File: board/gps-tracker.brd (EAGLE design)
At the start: 52.1 x 77.5 mm, 30 parts, among them J2 AVR_SPI_PRG_6OFFSET_PADS, U2 MCP73831, U3 ATMEGA328P, X1 USBSMD

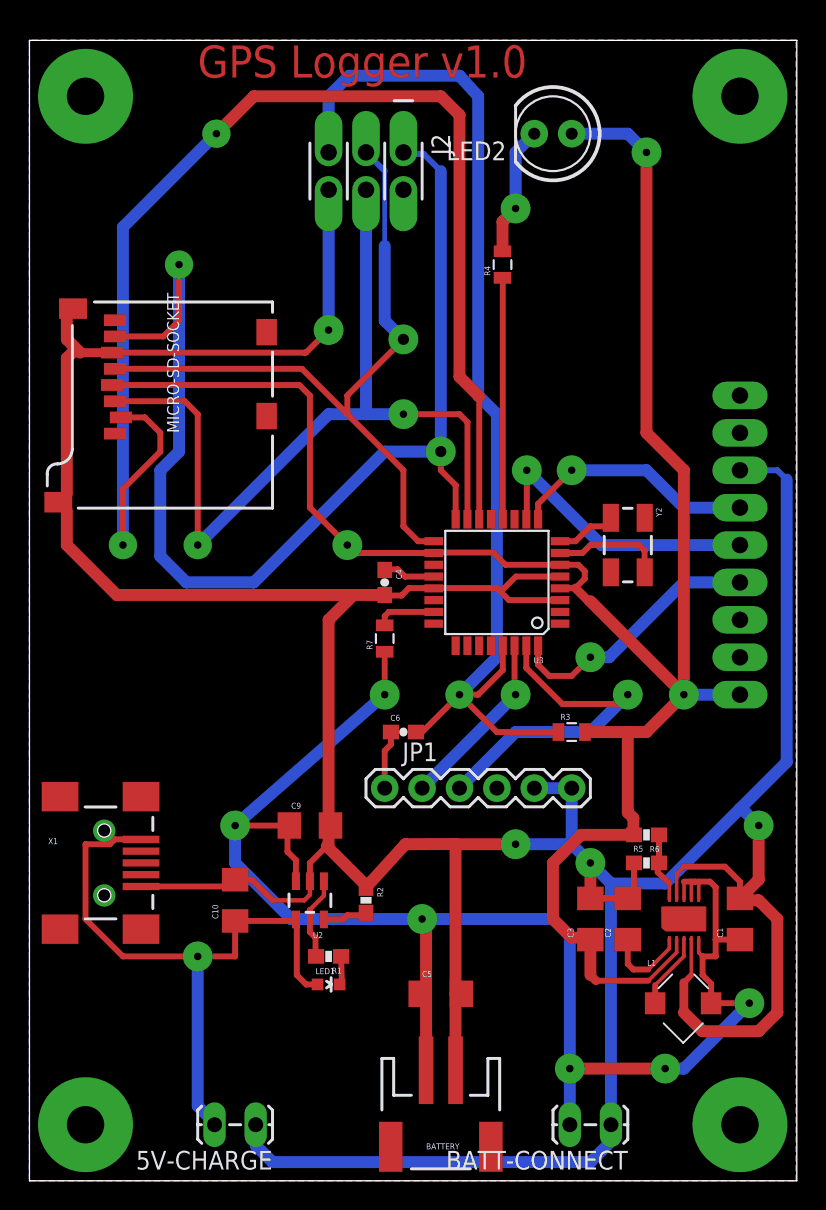
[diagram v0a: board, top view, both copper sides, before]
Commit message: Adding UVLO
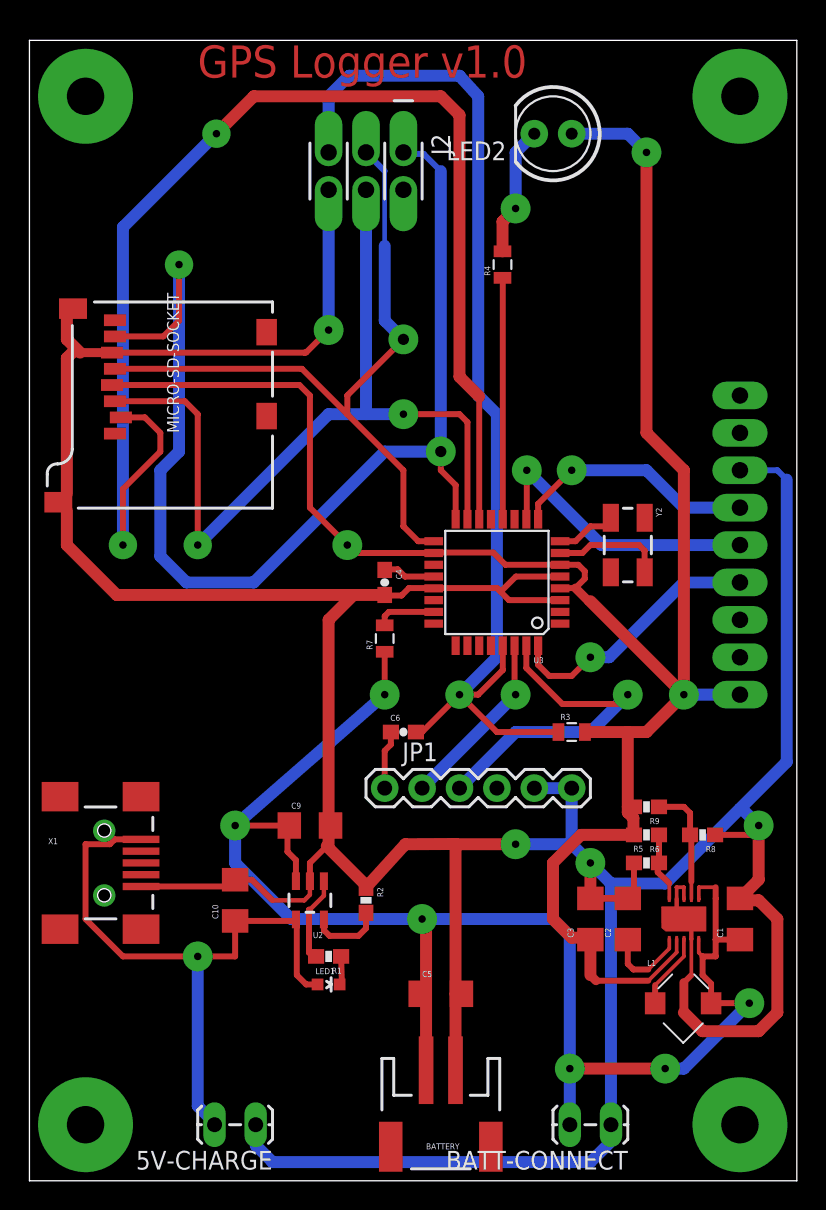
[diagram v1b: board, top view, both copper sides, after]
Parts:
- added R8: 250k, SparkFun:0603-RES
- added R9: 2M5, SparkFun:0603-RES
- R2: value 3k3 -> 2k
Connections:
- new net UVLO: R8.2, R9.1, U$1.7
- net 3.3V: now also R9.2
- net GND: now also R8.1, U$1.8
- net VBATT: no longer U$1.7, U$1.8
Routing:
- net UVLO: track 0.00 -> 8.17 mm
- net VBATT: track 110.1 -> 106.2 mm
- net N$6: track 3.06 -> 5.01 mm
- net GND: track 295.7 -> 296.4 mm
- removed copper zone on layer 1, net N$17
- removed copper zone on layer 16, net N$18
